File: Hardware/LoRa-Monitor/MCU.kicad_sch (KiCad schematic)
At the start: 45 parts, among them J2 Micro_SD_Card, U10 ESP32-S3-WROOM-1

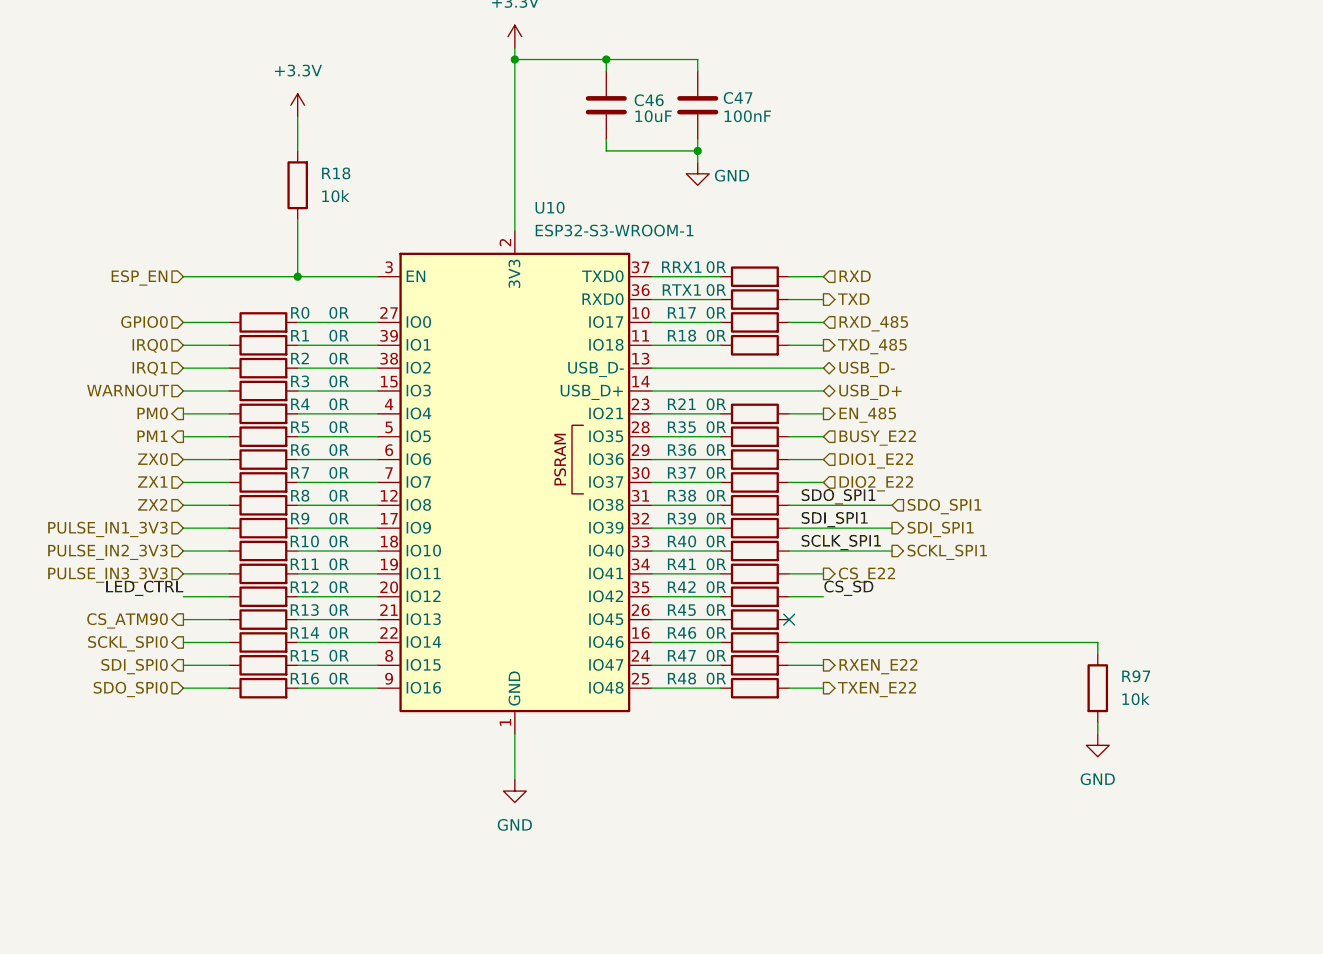
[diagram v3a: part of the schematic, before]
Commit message: Finished schematic, started with PCB design
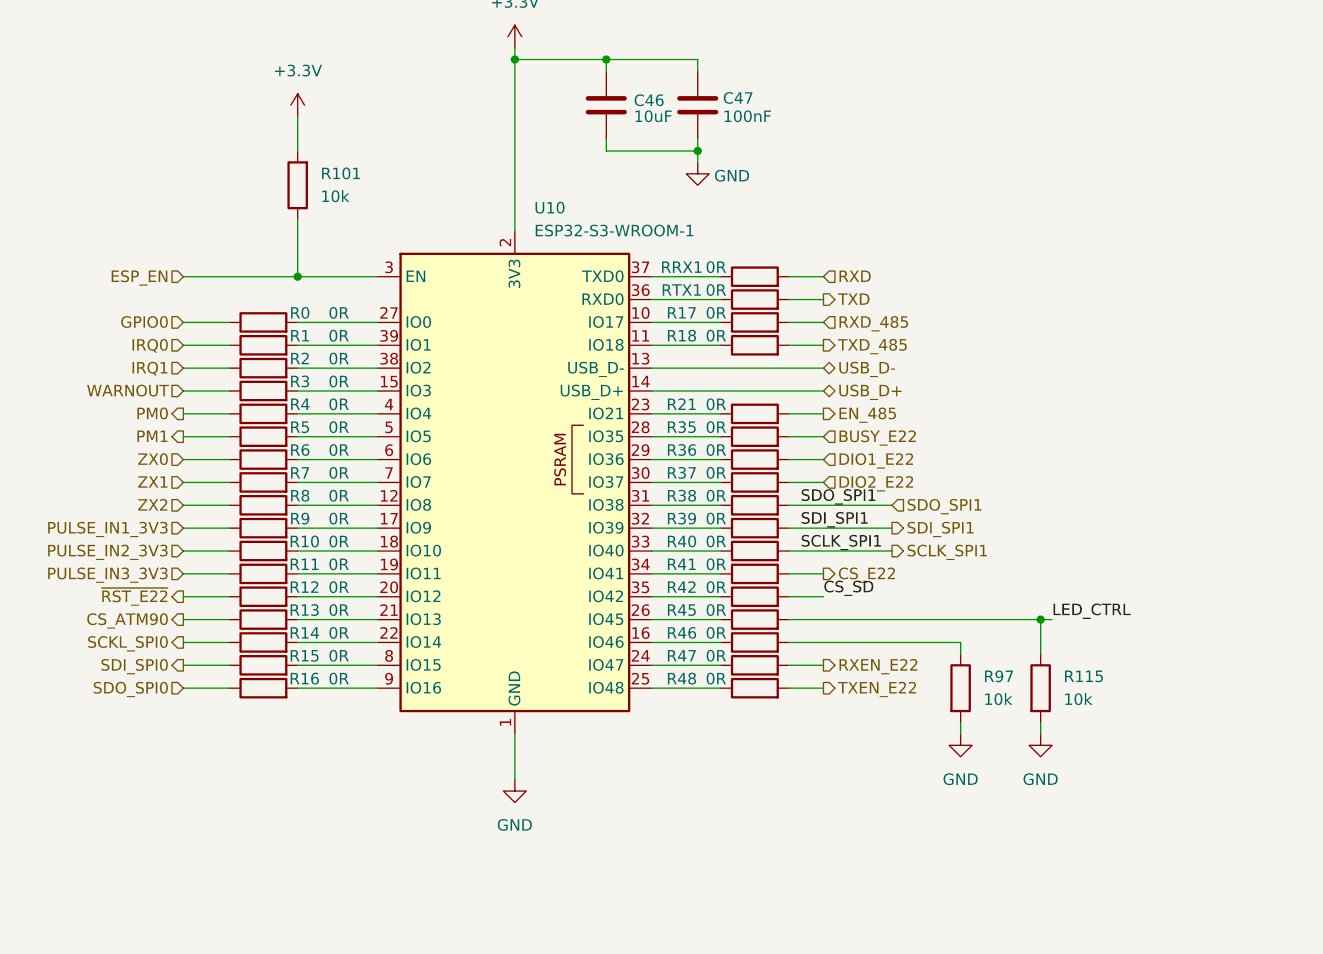
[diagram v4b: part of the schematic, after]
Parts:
- removed R18: 10k, Resistor_SMD:R_0805_2012Metric, symbol Device:R
- added R101, R115: 10k, Resistor_SMD:R_0805_2012Metric, symbol Device:R
- R0, R1, R10, R11, R12, R13, R14, R15, R16, R17, R18, R2, R21, R3, R35, R36, R37, R38, R39, R4, R40, R41, R42, R45, R46, R47, R48, R5, R6, R7, R8, R9, RRX1, RTX1: footprint Resistor_SMD:R_0805_2012Metric -> Resistor_SMD:R_0603_1608Metric
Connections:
- net +3.3V: now also R101.2
- net ESP_EN: now also R101.1
- net GND: now also R115.2
- net LED_CTRL: now also R45.2, R115.1; no longer R12.1
- net SCKL_SPI1 renamed SCLK_SPI1
- new net ~{RST_E22}: R12.1
- no-connect marks 4 -> 3
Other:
- moved on the sheet: R97

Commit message: Finished the first component disposition
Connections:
- net BUSY_E22: now also R16.1; no longer R35.2
- net CS_ATM90: now also R36.2; no longer R13.1
- net CS_E22: now also R7.1; no longer R41.2
- net CS_SD: now also R18.2; no longer R42.2
- net DIO1_E22: now also R17.2; no longer R36.2
- net DIO2_E22: now also R6.1; no longer R37.2
- net EN_485: now also R11.1; no longer R21.2
- net IRQ0: now also R40.2; no longer R1.1
- net IRQ1: now also R39.2; no longer R2.1
- net PM0: now also R38.2; no longer R4.1
- net PM1: now also R37.2; no longer R5.1
- net PULSE_IN1_3V3: now also R13.1; no longer R9.1
- net PULSE_IN2_3V3: now also R14.1; no longer R10.1
- net PULSE_IN3_3V3: now also R21.2; no longer R11.1
- net RXD_485: now also R12.1; no longer R17.2
- net RXEN_E22: now also R4.1; no longer R47.2
- net SCKL_SPI0: now also R35.2; no longer R14.1
- net SCLK_SPI1: now also R3.1; no longer R40.2
- net SDI_SPI0: now also R48.2; no longer R15.1
- net SDI_SPI1: now also R9.1; no longer R39.2
- net SDO_SPI0: now also R47.2; no longer R16.1
- net SDO_SPI1: now also R8.1; no longer R38.2
- net TXD_485: now also R10.1; no longer R18.2
- net TXEN_E22: now also R5.1; no longer R48.2
- net WARNOUT: now also R41.2; no longer R3.1
- net ZX0: now also R1.1; no longer R6.1
- net ZX1: now also R2.1; no longer R7.1
- net ZX2: now also R42.2; no longer R8.1
- net ~{RST_E22}: now also R15.1; no longer R12.1
